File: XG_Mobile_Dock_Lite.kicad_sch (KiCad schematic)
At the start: 20 parts, among them J1 5-1775443-8, J13 39300240, J14 469911008, J17 8730, J2 20455-040E-76, J3 20455-040E-76, J4 3-2362375-4, J5 USB_C_Receptacle, SW1 SW_Push

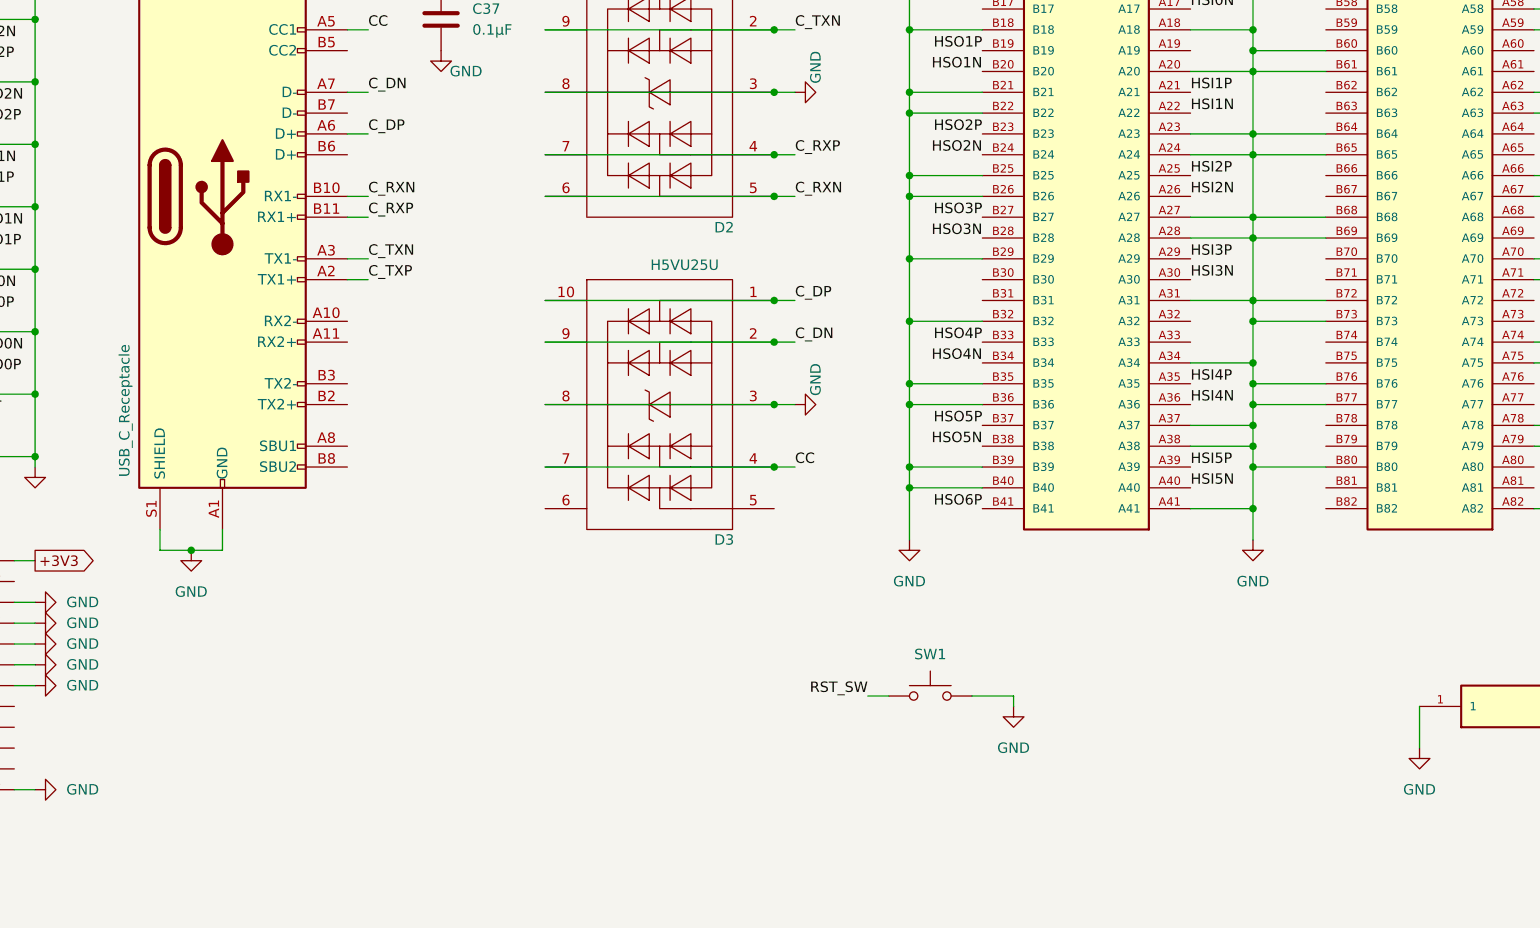
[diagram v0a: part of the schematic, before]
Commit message: added extra connector for ground from the cable
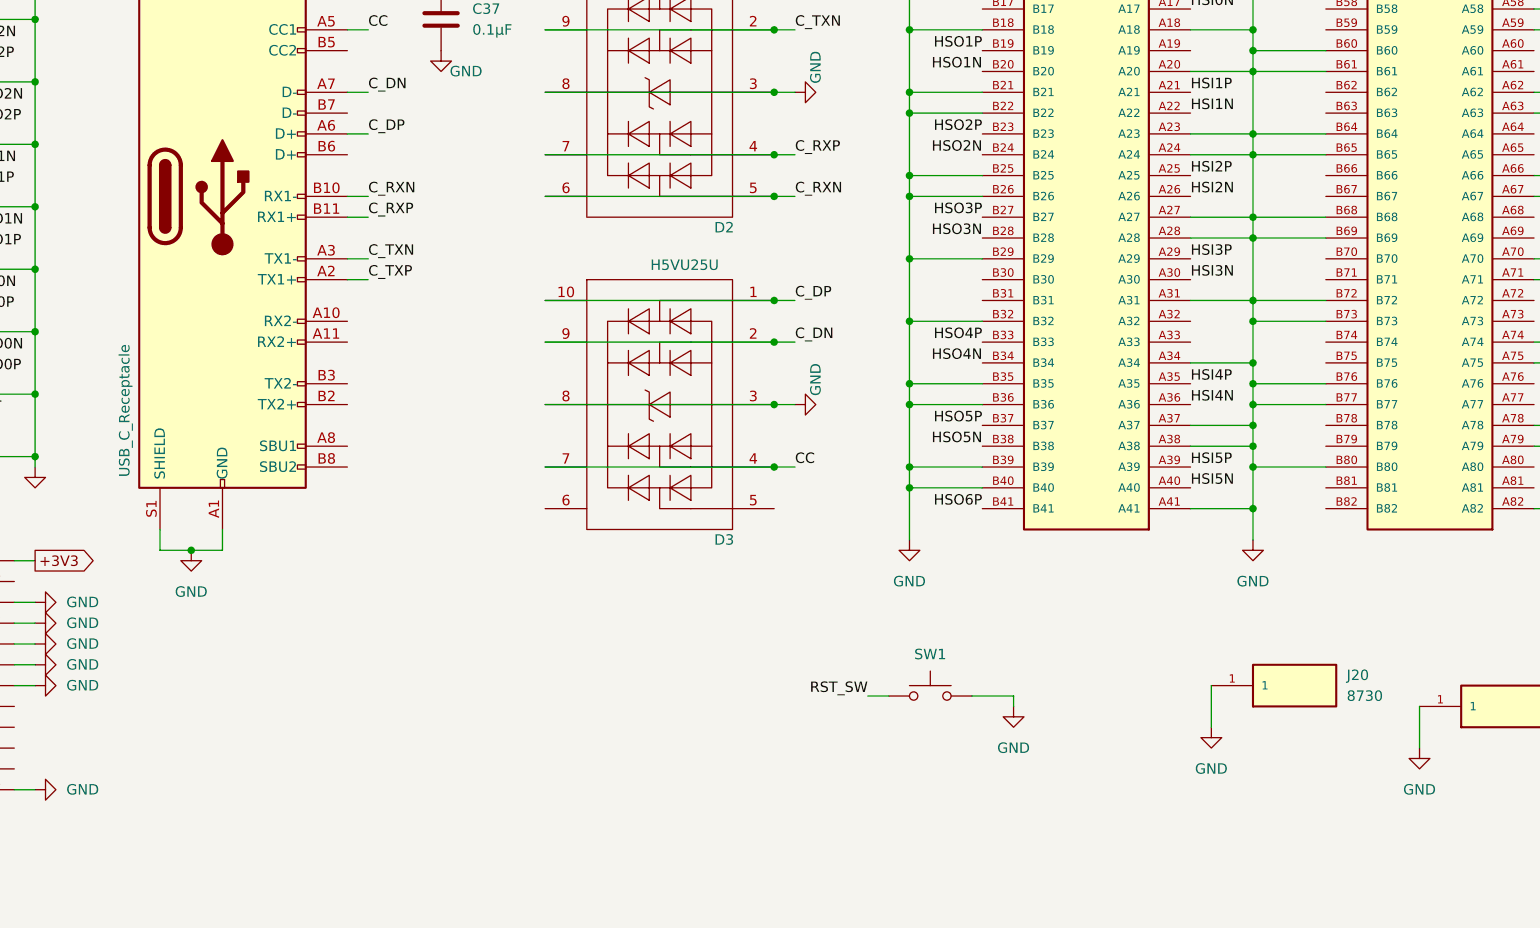
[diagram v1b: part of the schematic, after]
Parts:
- added J20: 8730, KEYSTONE_8730:KEYSTONE_8730, symbol KEYSTONE_8730:8730
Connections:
- net GND: now also J20.1

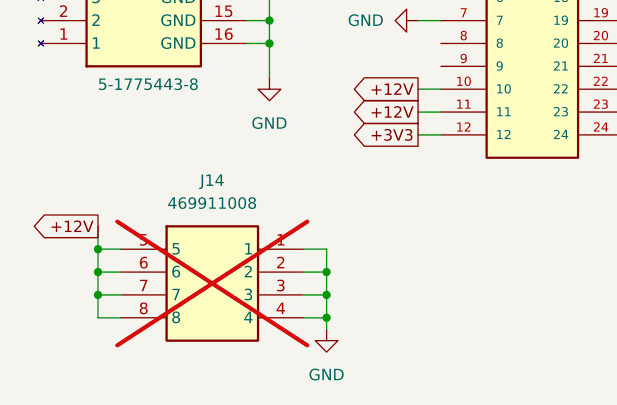
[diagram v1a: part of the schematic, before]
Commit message: added extra power connector
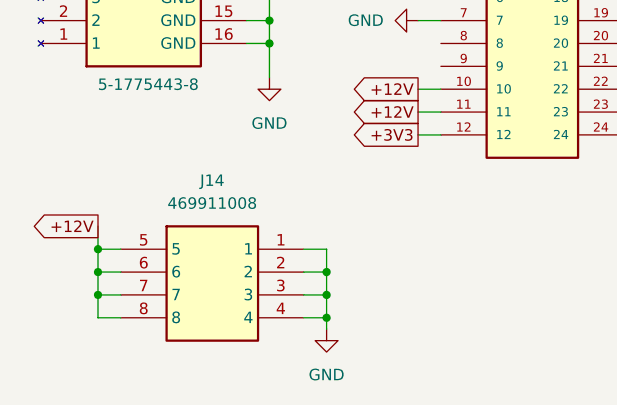
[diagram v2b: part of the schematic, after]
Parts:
- J14: now fitted; now in the parts list
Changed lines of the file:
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@@
 		(unit 1)
 		(exclude_from_sim no)
-		(in_bom no)
+		(in_bom yes)
 		(on_board yes)
-		(dnp yes)
+		(dnp no)
 		(fields_autoplaced yes)
 		(property "Reference" "J14"

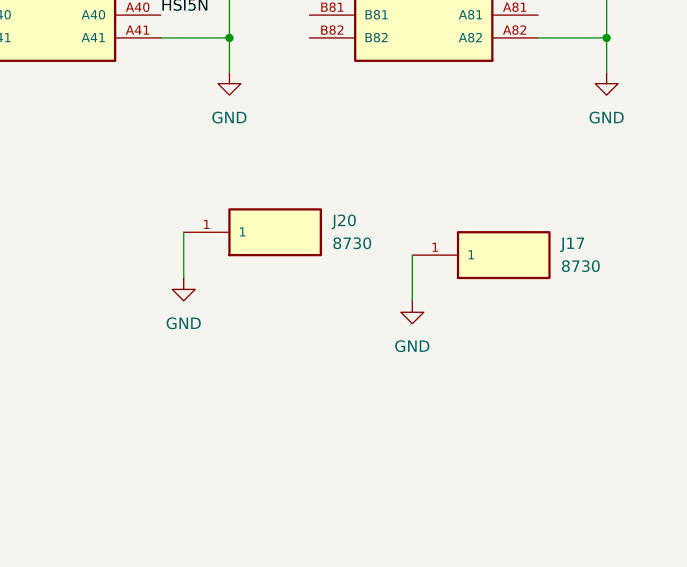
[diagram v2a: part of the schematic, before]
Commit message: added better ground screw
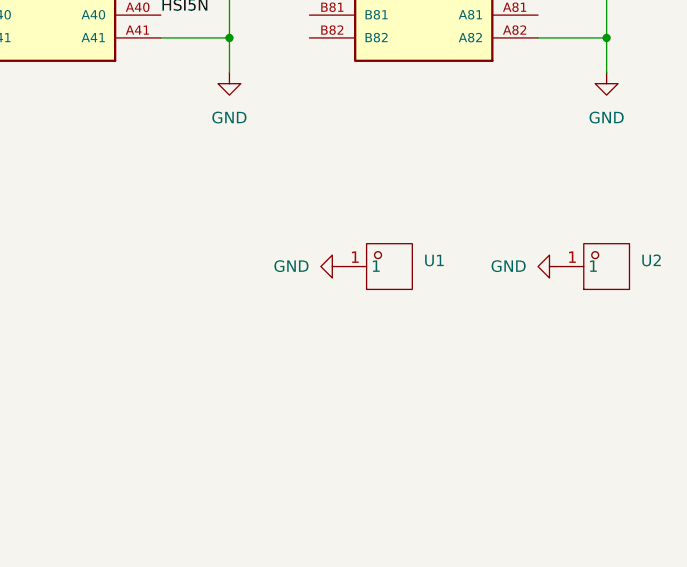
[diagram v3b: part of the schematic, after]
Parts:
- removed J17, J20: 8730, KEYSTONE_8730:KEYSTONE_8730, symbol KEYSTONE_8730:8730
- added U1, U2: ~, CONN-SMD_T31000:CONN-SMD_T31000, symbol T31000:T31000
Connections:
- net GND: now also U1.1, U2.1
